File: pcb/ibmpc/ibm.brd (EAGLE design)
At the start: 124 x 56 mm, 32 parts, among them J2 ATX24RH

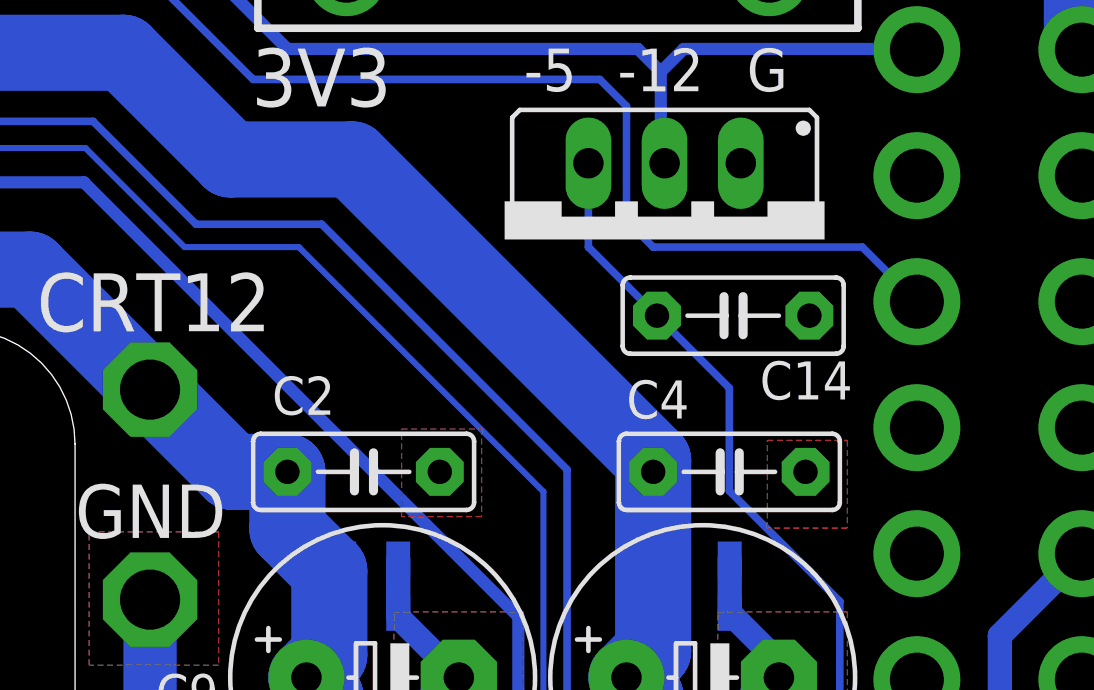
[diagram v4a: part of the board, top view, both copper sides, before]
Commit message: updated silkscreen
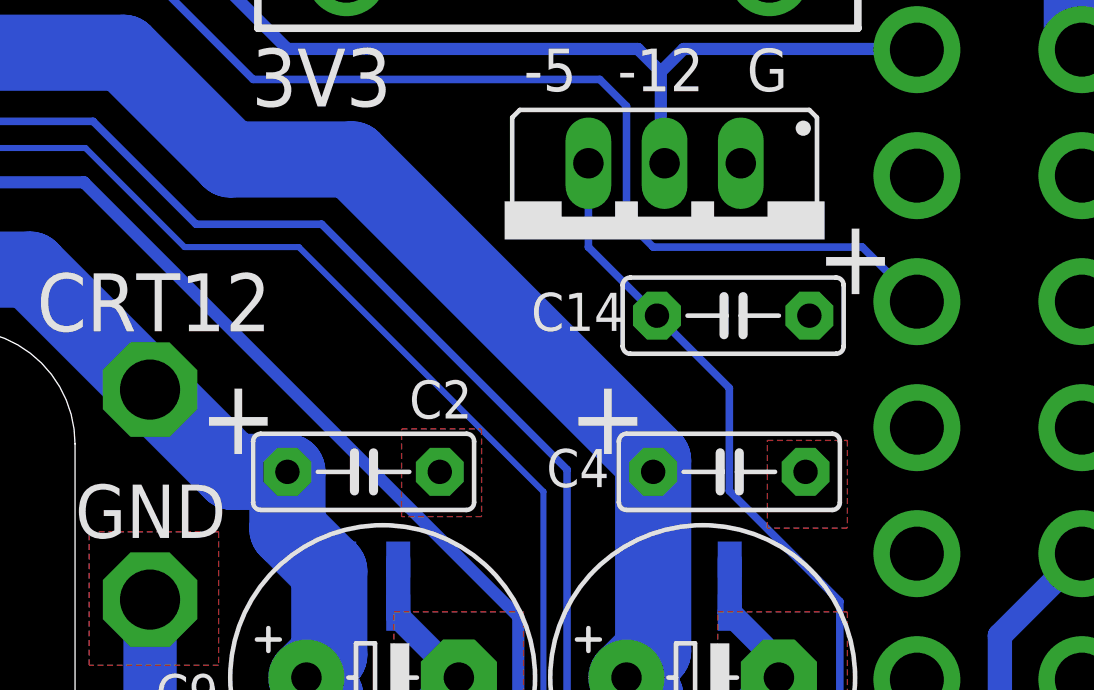
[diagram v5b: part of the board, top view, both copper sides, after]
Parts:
- R1: value (none) -> 470
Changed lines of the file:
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@@
 <setting verticaltext="up"/>
 </settings>
-<grid distance="5" unitdist="mil" unit="mm" style="lines" multiple="1" display="no" altdistance="1" altunitdist="mil" altunit="mil"/>
+<grid distance="5" unitdist="mil" unit="mil" style="lines" multiple="1" display="no" altdistance="1" altunitdist="mil" altunit="mil"/>
 <layers>
 <layer number="1" name="Top" color="4" fill="1" visible="yes" active="yes"/>
@@
 <text x="99.187" y="0.921" size="1.6764" layer="25" rot="R180" align="center">5V</text>
 <text x="80.042" y="14.097" size="2.1844" layer="25" distance="35" align="center">FAN</text>
+<text x="103.016" y="41.453" size="2.54" layer="25" rot="R180" align="center">+</text>
+<text x="94.761" y="36.119" size="2.54" layer="25" rot="R180" align="center">+</text>
+<text x="82.442" y="36.119" size="2.54" layer="25" rot="R180" align="center">+</text>
+<text x="29.737" y="54.534" size="2.54" layer="28" rot="R180" align="center">+</text>
 </plain>
 <attributes>
@@
 </element>
 <element name="C2" library="capacitor-wima" library_urn="urn:adsk.eagle:library:116" package="C5B2.5" package3d_urn="urn:adsk.eagle:package:5426/1" value="" x="86.619" y="34.258" smashed="yes">
-<attribute name="NAME" x="83.571" y="36.163" size="1.27" layer="25" ratio="10"/>
+<attribute name="NAME" x="88.143" y="36.036" size="1.27" layer="25" ratio="10"/>
 <attribute name="POPULARITY" value="10" x="86.619" y="34.258" size="1.778" layer="27" display="off"/>
 <attribute name="VALUE" x="84.587" y="31.464" size="1.27" layer="27" ratio="10"/>
@@
 </element>
 <element name="C4" library="capacitor-wima" library_urn="urn:adsk.eagle:library:116" package="C5B2.5" package3d_urn="urn:adsk.eagle:package:5426/1" value="" x="98.811" y="34.258" smashed="yes">
-<attribute name="NAME" x="95.382" y="36.036" size="1.27" layer="25" ratio="10"/>
+<attribute name="NAME" x="92.715" y="33.75" size="1.27" layer="25" ratio="10"/>
 <attribute name="POPULARITY" value="10" x="92.207" y="28.035" size="1.778" layer="27" display="off"/>
 <attribute name="VALUE" x="96.779" y="31.464" size="1.27" layer="27" ratio="10"/>
@@
 </element>
 <element name="C14" library="capacitor-wima" library_urn="urn:adsk.eagle:library:116" package="C5B2.5" package3d_urn="urn:adsk.eagle:package:5426/1" value="" x="98.938" y="39.465" smashed="yes">
-<attribute name="NAME" x="99.827" y="36.671" size="1.27" layer="25" ratio="10"/>
+<attribute name="NAME" x="92.207" y="38.957" size="1.27" layer="25" ratio="10"/>
 <attribute name="POPULARITY" value="10" x="98.938" y="40.481" size="1.778" layer="27" display="off"/>
 <attribute name="VALUE" x="96.906" y="36.671" size="1.27" layer="27" ratio="10"/>
@@
 <attribute name="VALUE" x="6.0536" y="23.2896" size="1.27" layer="27" ratio="10" rot="R270"/>
 </element>
-<element name="R1" library="adafruit" package="0207/10" value="" x="18.365" y="26.744" smashed="yes">
+<element name="R1" library="adafruit" package="0207/10" value="470" x="18.365" y="26.744" smashed="yes">
 <attribute name="NAME" x="15.317" y="23.95" size="1.27" layer="25" ratio="10"/>
 <attribute name="VALUE" x="16.1044" y="26.109" size="1.27" layer="27" ratio="10"/>

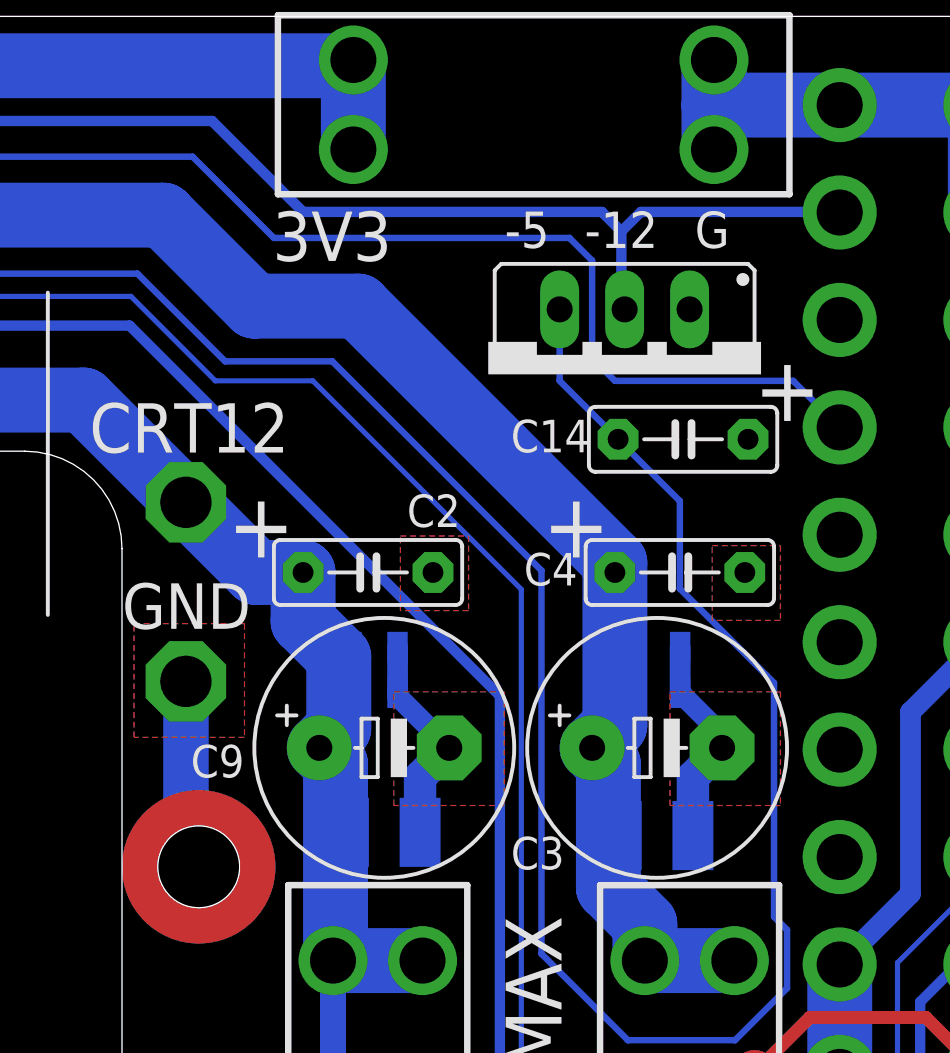
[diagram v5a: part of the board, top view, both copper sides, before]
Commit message: changed to 70L05
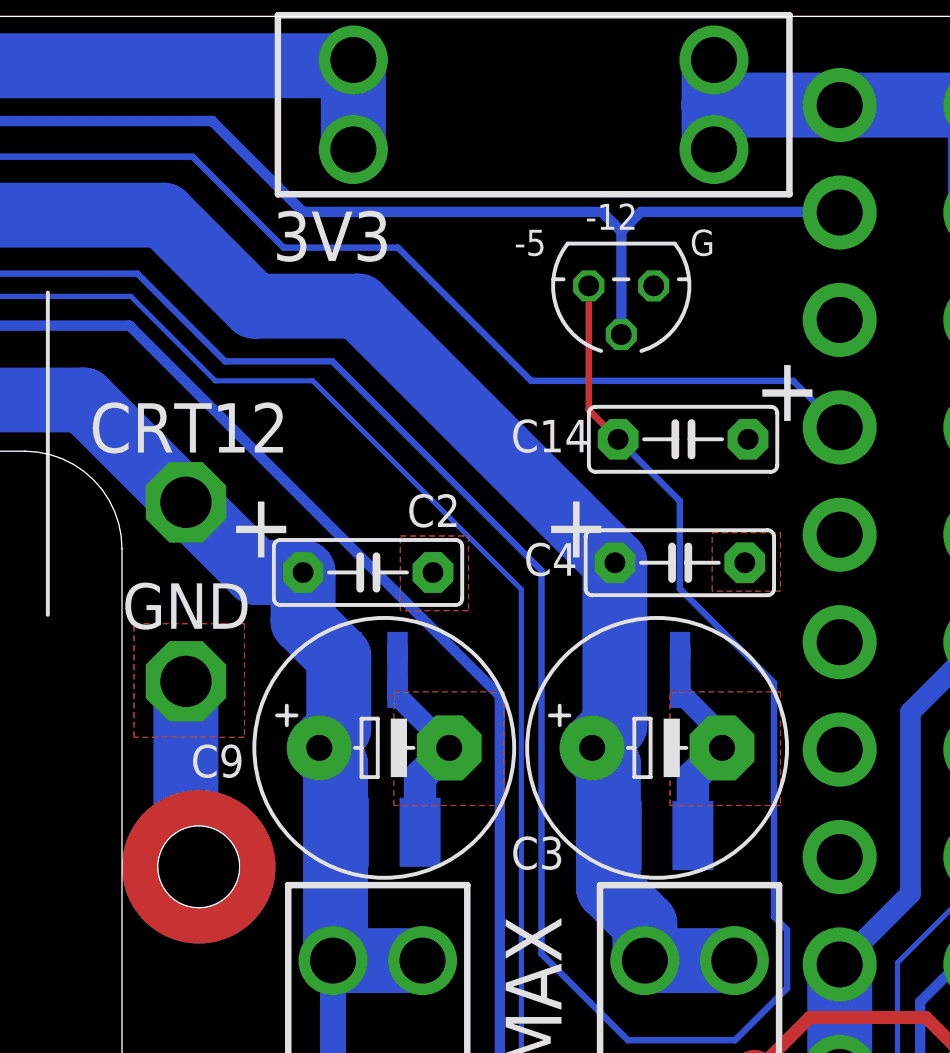
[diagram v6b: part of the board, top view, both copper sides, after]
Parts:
- removed IC1: (no value), v-reg:79XXS
- added IC2: (no value), linear:TO92
- moved C4 0.38 mm to (98.8, 34.6)
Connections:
- net GND: now also IC2.1; no longer IC1.GND
- net N$2: now also IC2.2; no longer IC1.IN
- net N$7: now also IC2.3; no longer IC1.OUT
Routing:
- net N$3: track 101.1 -> 98.9 mm
- net N$2: track 82.4 -> 83.3 mm
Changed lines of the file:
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@@
 <rectangle x1="67.823" y1="38.576" x2="72.014" y2="43.529" layer="41"/>
 <text x="15.6906" y="18.3234" size="2.54" layer="25" distance="35" align="center">picoRC.com</text>
-<text x="100.076" y="47.657" size="1.4224" layer="25" rot="R180" align="center">G</text>
-<text x="96.52" y="47.657" size="1.4224" layer="25" rot="R180" align="center">-12</text>
-<text x="92.837" y="47.657" size="1.4224" layer="25" rot="R180" align="center">-5</text>
+<text x="99.695" y="47.149" size="1.016" layer="25" rot="R180" align="center">G</text>
+<text x="96.139" y="48.165" size="1.016" layer="25" rot="R180" align="center">-12</text>
+<text x="92.964" y="47.149" size="1.016" layer="25" rot="R180" align="center">-5</text>
 <text x="85.217" y="47.403" size="1.9304" layer="25" rot="R180" align="center">3V3</text>
 <text x="87.122" y="0.921" size="1.6764" layer="25" rot="R180" align="center">12V</text>
@@
 <attribute name="VALUE" x="94.7978" y="24.1742" size="1.27" layer="27" ratio="10"/>
 </element>
-<element name="C4" library="capacitor-wima" library_urn="urn:adsk.eagle:library:116" package="C5B2.5" package3d_urn="urn:adsk.eagle:package:5426/1" value="" x="98.811" y="34.258" smashed="yes">
-<attribute name="NAME" x="92.715" y="33.75" size="1.27" layer="25" ratio="10"/>
-<attribute name="POPULARITY" value="10" x="92.207" y="28.035" size="1.778" layer="27" display="off"/>
-<attribute name="VALUE" x="96.779" y="31.464" size="1.27" layer="27" ratio="10"/>
+<element name="C4" library="capacitor-wima" library_urn="urn:adsk.eagle:library:116" package="C5B2.5" package3d_urn="urn:adsk.eagle:package:5426/1" value="" x="98.811" y="34.639" smashed="yes">
+<attribute name="NAME" x="92.715" y="34.131" size="1.27" layer="25" ratio="10"/>
+<attribute name="POPULARITY" value="10" x="92.207" y="28.416" size="1.778" layer="27" display="off"/>
+<attribute name="VALUE" x="96.779" y="31.845" size="1.27" layer="27" ratio="10"/>
 </element>
 <element name="C7" library="clock" package="0805@1" value="100nF" x="97.922" y="29.559" smashed="yes" rot="MR0">
@@
 <attribute name="NAME" x="18.3962" y="52.488" size="1.27" layer="25" ratio="10" rot="R270"/>
 <attribute name="VALUE" x="28.3072" y="54.1208" size="1.27" layer="27" ratio="10" rot="R180"/>
-</element>
-<element name="IC1" library="v-reg" library_urn="urn:adsk.eagle:library:409" package="79XXS" package3d_urn="urn:adsk.eagle:package:30343/1" value="" x="96.652" y="42.005" smashed="yes" rot="R180">
-<attribute name="POPULARITY" value="3" x="96.652" y="40.989" size="1.778" layer="27" rot="R180" display="off"/>
-<attribute name="VALUE" x="101.732" y="49.625" size="1.27" layer="27" ratio="10" rot="R180"/>
 </element>
 <element name="C14" library="capacitor-wima" library_urn="urn:adsk.eagle:library:116" package="C5B2.5" package3d_urn="urn:adsk.eagle:package:5426/1" value="" x="98.938" y="39.465" smashed="yes">
@@
 </element>
 <element name="U$7" library="apricot" package="M3_MOUNTING_HOLE_PACK" value="M3_MOUNTING_HOLE" x="80" y="22.75" smashed="yes"/>
+<element name="IC2" library="linear" library_urn="urn:adsk.eagle:library:262" package="TO92" package3d_urn="urn:adsk.eagle:package:16416/2" value="" x="96.52" y="45.466" smashed="yes" rot="R180">
+<attribute name="POPULARITY" value="0" x="96.52" y="45.466" size="1.778" layer="27" rot="R180" display="off"/>
+<attribute name="VALUE" x="93.599" y="46.736" size="1.27" layer="27" ratio="10" rot="R180"/>
+</element>
 </elements>
 <signals>
@@
 <contactref element="U$1" pad="P$7" route="any" routetag="G$1.GND"/>
 <contactref element="U$1" pad="P$17" route="any" routetag="G$1.GND"/>
-<contactref element="IC1" pad="GND"/>
 <contactref element="C14" pad="2"/>
 <contactref element="JP1" pad="2"/>
@@
 </polygon>
 <polygon width="0.1524" layer="1" thermals="no">
-<vertex x="100.076" y="35.306"/>
-<vertex x="102.743" y="35.306"/>
-<vertex x="102.743" y="32.385"/>
-<vertex x="100.076" y="32.385"/>
+<vertex x="100.076" y="35.814"/>
+<vertex x="102.743" y="35.814"/>
+<vertex x="102.743" y="33.528"/>
+<vertex x="100.076" y="33.528"/>
 </polygon>
 <polygon width="0.1524" layer="1" thermals="no">
@@
 <contactref element="U$7" pad="P$1"/>
 <contactref element="U$7" pad="P$2"/>
-<wire x1="79.5" y1="30" x2="79.5" y2="23.5" width="1.778" layer="16"/>
-<wire x1="79.5" y1="23.5" x2="80" y2="22.75" width="1.778" layer="16"/>
+<contactref element="IC2" pad="1"/>
+<wire x1="79.5" y1="30" x2="79.5" y2="23.25" width="2.54" layer="16"/>
+<wire x1="79.5" y1="23.25" x2="80" y2="22.75" width="2.54" layer="16"/>
 </signal>
 <signal name="+5V">
@@
 <contactref element="C7" pad="2"/>
 <contactref element="C5" pad="2"/>
-<wire x1="96.271" y1="34.258" x2="96.271" y2="28.289" width="2.54" layer="16"/>
+<wire x1="96.271" y1="34.639" x2="96.271" y2="28.289" width="2.54" layer="16"/>
 <wire x1="96.271" y1="28.289" x2="95.382" y2="27.4" width="2.54" layer="16"/>
 <wire x1="95.382" y1="27.4" x2="96.017" y2="26.765" width="2.54" layer="16"/>
@@
 <wire x1="97.442" y1="19.083" x2="100.942" y2="19.083" width="2.54" layer="16"/>
 <wire x1="96.271" y1="34.639" x2="86.238" y2="44.672" width="2.54" layer="16"/>
-<wire x1="96.271" y1="34.639" x2="96.271" y2="34.258" width="2.54" layer="16"/>
 <wire x1="78.618" y1="48.228" x2="82.174" y2="44.672" width="2.54" layer="16"/>
 <wire x1="82.174" y1="44.672" x2="86.238" y2="44.672" width="2.54" layer="16"/>
-<wire x1="96.271" y1="34.258" x2="97.022" y2="33.507" width="0.508" layer="16"/>
-<wire x1="97.022" y1="33.507" x2="97.022" y2="31.337" width="0.508" layer="16"/>
+<wire x1="96.271" y1="34.639" x2="97.022" y2="33.888" width="0.508" layer="16"/>
+<wire x1="97.022" y1="33.888" x2="97.022" y2="31.337" width="0.508" layer="16"/>
 <wire x1="97.022" y1="31.337" x2="97.022" y2="29.559" width="0.508" layer="16"/>
 <wire x1="97.022" y1="29.559" x2="97.022" y2="29.04" width="0.508" layer="16"/>
@@
 <contactref element="J2" pad="14"/>
 <contactref element="U$1" pad="P$12"/>
-<contactref element="IC1" pad="IN"/>
-<wire x1="96.525" y1="47.593" x2="96.525" y2="44.672" width="0.4064" layer="16"/>
-<wire x1="96.525" y1="44.672" x2="96.652" y2="44.545" width="0.4064" layer="16"/>
 <wire x1="105.061" y1="48.332" x2="105.038" y2="48.355" width="0.4064" layer="16"/>
 <wire x1="105.038" y1="48.355" x2="97.287" y2="48.355" width="0.4064" layer="16"/>
@@
 <wire x1="84.079" y1="48.355" x2="80.523" y2="51.911" width="0.4064" layer="16"/>
 <wire x1="80.523" y1="51.911" x2="40.55" y2="51.911" width="0.4064" layer="16"/>
+<contactref element="IC2" pad="2"/>
+<wire x1="96.525" y1="43.566" x2="96.52" y2="43.561" width="0.4064" layer="16"/>
+<wire x1="96.525" y1="47.593" x2="96.525" y2="43.566" width="0.4064" layer="16"/>
 </signal>
 <signal name="N$3">
@@
 <contactref element="U$1" pad="P$14"/>
 <wire x1="105.061" y1="39.932" x2="103.242" y2="41.751" width="0.254" layer="16"/>
-<wire x1="103.242" y1="41.751" x2="96.271" y2="41.751" width="0.254" layer="16"/>
-<wire x1="96.271" y1="41.751" x2="95.382" y2="42.64" width="0.254" layer="16"/>
-<wire x1="95.382" y1="46.45" x2="94.493" y2="47.339" width="0.254" layer="16"/>
-<wire x1="94.493" y1="47.339" x2="82.936" y2="47.339" width="0.254" layer="16"/>
-<wire x1="95.382" y1="42.64" x2="95.382" y2="46.45" width="0.254" layer="16"/>
 <wire x1="41.439" y1="48.99" x2="41.439" y2="45.434" width="0.254" layer="16"/>
 <via x="41.439" y="45.434" extent="1-16" drill="0.55"/>
 <wire x1="41.439" y1="45.434" x2="42.328" y2="45.434" width="0.254" layer="1"/>
 <wire x1="44.7" y1="43.062" x2="44.7" y2="41" width="0.254" layer="1"/>
-<wire x1="82.936" y1="47.339" x2="79.761" y2="50.514" width="0.254" layer="16"/>
+<wire x1="83.317" y1="46.958" x2="79.761" y2="50.514" width="0.254" layer="16"/>
 <wire x1="79.761" y1="50.514" x2="42.963" y2="50.514" width="0.254" layer="16"/>
 <wire x1="42.963" y1="50.514" x2="41.439" y2="48.99" width="0.254" layer="16"/>
@@
 <wire x1="28.39" y1="39.783" x2="24.633" y2="39.783" width="0.2032" layer="1"/>
 <wire x1="29.596" y1="40.989" x2="28.39" y2="39.783" width="0.2032" layer="1"/>
+<wire x1="87.789" y1="46.958" x2="83.317" y2="46.958" width="0.254" layer="16"/>
+<wire x1="103.242" y1="41.751" x2="92.996" y2="41.751" width="0.254" layer="16"/>
+<wire x1="92.996" y1="41.751" x2="87.789" y2="46.958" width="0.254" layer="16"/>
 </signal>
 <signal name="N$4">
@@
 </signal>
 <signal name="N$7">
-<contactref element="IC1" pad="OUT"/>
 <contactref element="U$1" pad="P$18"/>
 <contactref element="C14" pad="1"/>
-<wire x1="94.112" y1="44.545" x2="94.112" y2="41.751" width="0.254" layer="16"/>
-<wire x1="94.112" y1="41.751" x2="96.398" y2="39.465" width="0.254" layer="16"/>
 <wire x1="96.398" y1="39.465" x2="98.811" y2="37.052" width="0.254" layer="16"/>
 <wire x1="102.494" y1="20.796" x2="103.002" y2="20.288" width="0.254" layer="16"/>
@@
 <wire x1="77.602" y1="45.942" x2="81.031" y2="42.513" width="0.254" layer="16"/>
 <wire x1="81.031" y1="42.513" x2="85.222" y2="42.513" width="0.254" layer="16"/>
+<contactref element="IC2" pad="3"/>
+<wire x1="95.25" y1="45.466" x2="95.25" y2="40.613" width="0.254" layer="1"/>
+<wire x1="95.25" y1="40.613" x2="96.398" y2="39.465" width="0.254" layer="1"/>
 </signal>
 <signal name="N$9">
